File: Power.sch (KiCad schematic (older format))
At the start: 53 parts, among them J1 Conn_01x02, J2 Conn_01x02, U2 A4403, U3 TPS54531, U4 AP7361C-33E-13

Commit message: added resistor numbers
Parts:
- gave numbers to parts that had none: 34

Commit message: small revisions
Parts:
- removed D6: D_Schottky, symbol Device:D_Schottky
- added JP?: Jumper_3_Open, symbol Jumper:Jumper_3_Open
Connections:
- net labels added: 5V_INT
- wire segments 203 -> 204
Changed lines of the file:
@@
 	0    1    1    0
 $EndComp
-Wire Wire Line
-	9250 3900 9400 3900
 Connection ~ 9250 3900
-$Comp
-L power:+5V #PWR038
-U 1 1 5FBBF8B1
-P 10100 3850
-F 0 "#PWR038" H 10100 3700 50  0001 C CNN
-F 1 "+5V" H 10115 4023 50  0000 C CNN
-F 2 "" H 10100 3850 50  0001 C CNN
-F 3 "" H 10100 3850 50  0001 C CNN
-	1    10100 3850
-	1    0    0    -1
-$EndComp
-Wire Wire Line
-	10100 3850 10100 3900
 Wire Wire Line
 	10100 3900 9850 3900
-$Comp
-L Device:D_Schottky D6
-U 1 1 5FBC1E83
-P 9050 3650
-F 0 "D6" H 9050 3433 50  0000 C CNN
-F 1 "D_Schottky" H 9050 3524 50  0000 C CNN
-F 2 "" H 9050 3650 50  0001 C CNN
-F 3 "~" H 9050 3650 50  0001 C CNN
-	1    9050 3650
-	-1   0    0    1
-$EndComp
-Wire Wire Line
-	9200 3650 9400 3650
-Wire Wire Line
-	9400 3650 9400 3900
-Connection ~ 9400 3900
-Wire Wire Line
-	9400 3900 9550 3900
-Text GLabel 8700 3650 0    50   Input ~ 0
-5V_USB
-Wire Wire Line
-	8700 3650 8900 3650
 $Comp
 L power:+5V #PWR032
@@
 	9750 1100 9750 1000
 Connection ~ 9450 1100
+Text GLabel 10100 3900 2    50   Input ~ 0
+5V_INT
+$Comp
+L power:+5V #PWR?
+U 1 1 5FA47275
+P 10350 2950
+F 0 "#PWR?" H 10350 2800 50  0001 C CNN
+F 1 "+5V" H 10365 3123 50  0000 C CNN
+F 2 "" H 10350 2950 50  0001 C CNN
+F 3 "" H 10350 2950 50  0001 C CNN
+	1    10350 2950
+	1    0    0    -1
+$EndComp
+$Comp
+L Jumper:Jumper_3_Open JP?
+U 1 1 5FA47DE8
+P 9950 3050
+F 0 "JP?" V 9996 3137 50  0000 L CNN
+F 1 "Jumper_3_Open" V 9905 3137 50  0000 L CNN
+F 2 "" H 9950 3050 50  0001 C CNN
+F 3 "~" H 9950 3050 50  0001 C CNN
+	1    9950 3050
+	0    -1   -1   0
+$EndComp
+Text GLabel 9850 3450 0    50   Input ~ 0
+5V_USB
+Text GLabel 9850 2700 0    50   Input ~ 0
+5V_INT
+Wire Wire Line
+	9850 3450 9950 3450
+Wire Wire Line
+	9950 3450 9950 3300
+Wire Wire Line
+	9950 2800 9950 2700
+Wire Wire Line
+	9950 2700 9850 2700
+Wire Wire Line
+	10100 3050 10350 3050
+Wire Wire Line
+	10350 3050 10350 2950
+Wire Wire Line
+	9250 3900 9550 3900
 $EndSCHEMATC

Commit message: Completed Labelling of Schematic - All nets attached
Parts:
- added D? (x3): LED, symbol Device:LED
- added R? (x3): 2.2k, symbol Device:R_US
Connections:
- wire segments 204 -> 216
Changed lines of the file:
@@
 Wire Wire Line
 	9250 3900 9550 3900
+$Comp
+L Device:LED D?
+U 1 1 604875E7
+P 1700 5650
+F 0 "D?" V 1739 5532 50  0000 R CNN
+F 1 "LED" V 1648 5532 50  0000 R CNN
+F 2 "" H 1700 5650 50  0001 C CNN
+F 3 "~" H 1700 5650 50  0001 C CNN
+	1    1700 5650
+	0    -1   -1   0
+$EndComp
+$Comp
+L Device:R_US R?
+U 1 1 604887E0
+P 1700 5250
+F 0 "R?" H 1768 5296 50  0000 L CNN
+F 1 "2.2k" H 1768 5205 50  0000 L CNN
+F 2 "" V 1740 5240 50  0001 C CNN
+F 3 "~" H 1700 5250 50  0001 C CNN
+	1    1700 5250
+	1    0    0    -1
+$EndComp
+$Comp
+L power:GND #PWR?
+U 1 1 60488EDC
+P 1700 5950
+F 0 "#PWR?" H 1700 5700 50  0001 C CNN
+F 1 "GND" H 1705 5777 50  0000 C CNN
+F 2 "" H 1700 5950 50  0001 C CNN
+F 3 "" H 1700 5950 50  0001 C CNN
+	1    1700 5950
+	1    0    0    -1
+$EndComp
+Wire Wire Line
+	1700 5950 1700 5800
+Wire Wire Line
+	1700 5500 1700 5400
+$Comp
+L Device:LED D?
+U 1 1 604A7613
+P 2150 5650
+F 0 "D?" V 2189 5532 50  0000 R CNN
+F 1 "LED" V 2098 5532 50  0000 R CNN
+F 2 "" H 2150 5650 50  0001 C CNN
+F 3 "~" H 2150 5650 50  0001 C CNN
+	1    2150 5650
+	0    -1   -1   0
+$EndComp
+$Comp
+L Device:R_US R?
+U 1 1 604A7619
+P 2150 5250
+F 0 "R?" H 2218 5296 50  0000 L CNN
+F 1 "2.2k" H 2218 5205 50  0000 L CNN
+F 2 "" V 2190 5240 50  0001 C CNN
+F 3 "~" H 2150 5250 50  0001 C CNN
+	1    2150 5250
+	1    0    0    -1
+$EndComp
+$Comp
+L power:GND #PWR?
+U 1 1 604A761F
+P 2150 5950
+F 0 "#PWR?" H 2150 5700 50  0001 C CNN
+F 1 "GND" H 2155 5777 50  0000 C CNN
+F 2 "" H 2150 5950 50  0001 C CNN
+F 3 "" H 2150 5950 50  0001 C CNN
+	1    2150 5950
+	1    0    0    -1
+$EndComp
+Wire Wire Line
+	2150 5950 2150 5800
+Wire Wire Line
+	2150 5500 2150 5400
+$Comp
+L Device:LED D?
+U 1 1 604B1E4C
+P 2550 5650
+F 0 "D?" V 2589 5532 50  0000 R CNN
+F 1 "LED" V 2498 5532 50  0000 R CNN
+F 2 "" H 2550 5650 50  0001 C CNN
+F 3 "~" H 2550 5650 50  0001 C CNN
+	1    2550 5650
+	0    -1   -1   0
+$EndComp
+$Comp
+L Device:R_US R?
+U 1 1 604B1E52
+P 2550 5250
+F 0 "R?" H 2618 5296 50  0000 L CNN
+F 1 "2.2k" H 2618 5205 50  0000 L CNN
+F 2 "" V 2590 5240 50  0001 C CNN
+F 3 "~" H 2550 5250 50  0001 C CNN
+	1    2550 5250
+	1    0    0    -1
+$EndComp
+$Comp
+L power:GND #PWR?
+U 1 1 604B1E58
+P 2550 5950
+F 0 "#PWR?" H 2550 5700 50  0001 C CNN
+F 1 "GND" H 2555 5777 50  0000 C CNN
+F 2 "" H 2550 5950 50  0001 C CNN
+F 3 "" H 2550 5950 50  0001 C CNN
+	1    2550 5950
+	1    0    0    -1
+$EndComp
+Wire Wire Line
+	2550 5950 2550 5800
+Wire Wire Line
+	2550 5500 2550 5400
+Text GLabel 1650 4850 0    50   Input ~ 0
+VIN
+Wire Wire Line
+	1650 4850 1700 4850
+Wire Wire Line
+	1700 4850 1700 5100
+Text GLabel 2050 4700 0    50   Input ~ 0
+VIN_BED
+Wire Wire Line
+	2050 4700 2150 4700
+Wire Wire Line
+	2150 4700 2150 5100
+Text GLabel 2450 4600 0    50   Input ~ 0
+5V_USB
+Wire Wire Line
+	2450 4600 2550 4600
+Wire Wire Line
+	2550 4600 2550 5100
 $EndSCHEMATC

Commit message: added raspberry pi header
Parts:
- gave numbers to parts that had none: 7
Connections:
- no-connect marks 0 -> 1
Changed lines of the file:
@@
 5V_INT
 $Comp
-L power:+5V #PWR?
+L power:+5V #PWR0157
 U 1 1 5FA47275
 P 10350 2950
-F 0 "#PWR?" H 10350 2800 50  0001 C CNN
+F 0 "#PWR0157" H 10350 2800 50  0001 C CNN
 F 1 "+5V" H 10365 3123 50  0000 C CNN
 F 2 "" H 10350 2950 50  0001 C CNN
@@
 $EndComp
 $Comp
-L Jumper:Jumper_3_Open JP?
+L Jumper:Jumper_3_Open JP22
 U 1 1 5FA47DE8
 P 9950 3050
-F 0 "JP?" V 9996 3137 50  0000 L CNN
+F 0 "JP22" V 9996 3137 50  0000 L CNN
 F 1 "Jumper_3_Open" V 9905 3137 50  0000 L CNN
 F 2 "" H 9950 3050 50  0001 C CNN
@@
 	9250 3900 9550 3900
 $Comp
-L Device:LED D?
+L Device:LED D6
 U 1 1 604875E7
 P 1700 5650
-F 0 "D?" V 1739 5532 50  0000 R CNN
+F 0 "D6" V 1739 5532 50  0000 R CNN
 F 1 "LED" V 1648 5532 50  0000 R CNN
 F 2 "" H 1700 5650 50  0001 C CNN
@@
 $EndComp
 $Comp
-L Device:R_US R?
+L Device:R_US R66
 U 1 1 604887E0
 P 1700 5250
-F 0 "R?" H 1768 5296 50  0000 L CNN
+F 0 "R66" H 1768 5296 50  0000 L CNN
 F 1 "2.2k" H 1768 5205 50  0000 L CNN
 F 2 "" V 1740 5240 50  0001 C CNN
@@
 $EndComp
 $Comp
-L power:GND #PWR?
+L power:GND #PWR038
 U 1 1 60488EDC
 P 1700 5950
-F 0 "#PWR?" H 1700 5700 50  0001 C CNN
+F 0 "#PWR038" H 1700 5700 50  0001 C CNN
 F 1 "GND" H 1705 5777 50  0000 C CNN
 F 2 "" H 1700 5950 50  0001 C CNN
@@
 	1700 5500 1700 5400
 $Comp
-L Device:LED D?
+L Device:LED D7
 U 1 1 604A7613
 P 2150 5650
-F 0 "D?" V 2189 5532 50  0000 R CNN
+F 0 "D7" V 2189 5532 50  0000 R CNN
 F 1 "LED" V 2098 5532 50  0000 R CNN
 F 2 "" H 2150 5650 50  0001 C CNN
@@
 $EndComp
 $Comp
-L Device:R_US R?
+L Device:R_US R67
 U 1 1 604A7619
 P 2150 5250
-F 0 "R?" H 2218 5296 50  0000 L CNN
+F 0 "R67" H 2218 5296 50  0000 L CNN
 F 1 "2.2k" H 2218 5205 50  0000 L CNN
 F 2 "" V 2190 5240 50  0001 C CNN
@@
 $EndComp
 $Comp
-L power:GND #PWR?
+L power:GND #PWR0155
 U 1 1 604A761F
 P 2150 5950
-F 0 "#PWR?" H 2150 5700 50  0001 C CNN
+F 0 "#PWR0155" H 2150 5700 50  0001 C CNN
 F 1 "GND" H 2155 5777 50  0000 C CNN
 F 2 "" H 2150 5950 50  0001 C CNN
@@
 	2150 5500 2150 5400
 $Comp
-L Device:LED D?
+L Device:LED D8
 U 1 1 604B1E4C
 P 2550 5650
-F 0 "D?" V 2589 5532 50  0000 R CNN
+F 0 "D8" V 2589 5532 50  0000 R CNN
 F 1 "LED" V 2498 5532 50  0000 R CNN
 F 2 "" H 2550 5650 50  0001 C CNN
@@
 $EndComp
 $Comp
-L Device:R_US R?
+L Device:R_US R68
 U 1 1 604B1E52
 P 2550 5250
-F 0 "R?" H 2618 5296 50  0000 L CNN
+F 0 "R68" H 2618 5296 50  0000 L CNN
 F 1 "2.2k" H 2618 5205 50  0000 L CNN
 F 2 "" V 2590 5240 50  0001 C CNN
@@
 $EndComp
 $Comp
-L power:GND #PWR?
+L power:GND #PWR0156
 U 1 1 604B1E58
 P 2550 5950
-F 0 "#PWR?" H 2550 5700 50  0001 C CNN
+F 0 "#PWR0156" H 2550 5700 50  0001 C CNN
 F 1 "GND" H 2555 5777 50  0000 C CNN
 F 2 "" H 2550 5950 50  0001 C CNN
@@
 Wire Wire Line
 	2550 4600 2550 5100
+NoConn ~ 6400 4050
 $EndSCHEMATC

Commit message: assigned some footprints
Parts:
- C24, C25, C26, C27, C28, C29, C32, C38, C41, C53: footprint (none) -> Capacitor_SMD:C_0603_1608Metric_Pad1.05x0.95mm_HandSolder
- C36: footprint (none) -> Capacitor_SMD:CP_Elec_6.3x7.7
- C37, C42, C46, C50, C52: footprint (none) -> Capacitor_SMD:C_0805_2012Metric_Pad1.15x1.40mm_HandSolder
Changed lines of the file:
@@
 F 0 "C24" H 1892 2496 50  0000 L CNN
 F 1 "100nF" H 1892 2405 50  0000 L CNN
-F 2 "" H 1800 2450 50  0001 C CNN
+F 2 "Capacitor_SMD:C_0603_1608Metric_Pad1.05x0.95mm_HandSolder" H 1800 2450 50  0001 C CNN
 F 3 "~" H 1800 2450 50  0001 C CNN
 	1    1800 2450
@@
 F 0 "C27" H 2492 2496 50  0000 L CNN
 F 1 "100nF" H 2492 2405 50  0000 L CNN
-F 2 "" H 2400 2450 50  0001 C CNN
+F 2 "Capacitor_SMD:C_0603_1608Metric_Pad1.05x0.95mm_HandSolder" H 2400 2450 50  0001 C CNN
 F 3 "~" H 2400 2450 50  0001 C CNN
 	1    2400 2450
@@
 F 0 "C26" H 1892 4046 50  0000 L CNN
 F 1 "100nF" H 1892 3955 50  0000 L CNN
-F 2 "" H 1800 4000 50  0001 C CNN
+F 2 "Capacitor_SMD:C_0603_1608Metric_Pad1.05x0.95mm_HandSolder" H 1800 4000 50  0001 C CNN
 F 3 "~" H 1800 4000 50  0001 C CNN
 	1    1800 4000
@@
 F 0 "C29" H 2492 4046 50  0000 L CNN
 F 1 "100nF" H 2492 3955 50  0000 L CNN
-F 2 "" H 2400 4000 50  0001 C CNN
+F 2 "Capacitor_SMD:C_0603_1608Metric_Pad1.05x0.95mm_HandSolder" H 2400 4000 50  0001 C CNN
 F 3 "~" H 2400 4000 50  0001 C CNN
 	1    2400 4000
@@
 F 0 "C25" H 1892 3246 50  0000 L CNN
 F 1 "100nF" H 1892 3155 50  0000 L CNN
-F 2 "" H 1800 3200 50  0001 C CNN
+F 2 "Capacitor_SMD:C_0603_1608Metric_Pad1.05x0.95mm_HandSolder" H 1800 3200 50  0001 C CNN
 F 3 "~" H 1800 3200 50  0001 C CNN
 	1    1800 3200
@@
 F 0 "C28" H 2492 3246 50  0000 L CNN
 F 1 "100nF" H 2492 3155 50  0000 L CNN
-F 2 "" H 2400 3200 50  0001 C CNN
+F 2 "Capacitor_SMD:C_0603_1608Metric_Pad1.05x0.95mm_HandSolder" H 2400 3200 50  0001 C CNN
 F 3 "~" H 2400 3200 50  0001 C CNN
 	1    2400 3200
@@
 F 0 "C32" V 5592 4146 50  0000 L BNN
 F 1 "100nF" V 5592 4055 50  0000 R BNN
-F 2 "" H 5500 4100 50  0001 C CNN
+F 2 "Capacitor_SMD:C_0603_1608Metric_Pad1.05x0.95mm_HandSolder" H 5500 4100 50  0001 C CNN
 F 3 "~" H 5500 4100 50  0001 C CNN
 	1    5500 4100
@@
 F 0 "C42" V 6192 5996 50  0000 L BNN
 F 1 "10uF" V 6192 5905 50  0000 R BNN
-F 2 "" H 6100 5950 50  0001 C CNN
+F 2 "Capacitor_SMD:C_0805_2012Metric_Pad1.15x1.40mm_HandSolder" H 6100 5950 50  0001 C CNN
 F 3 "~" H 6100 5950 50  0001 C CNN
 	1    6100 5950
@@
 F 0 "C46" V 7692 5996 50  0000 L BNN
 F 1 "10uF" V 7692 5905 50  0000 R BNN
-F 2 "" H 7600 5950 50  0001 C CNN
+F 2 "Capacitor_SMD:C_0805_2012Metric_Pad1.15x1.40mm_HandSolder" H 7600 5950 50  0001 C CNN
 F 3 "~" H 7600 5950 50  0001 C CNN
 	1    7600 5950
@@
 F 0 "C37" V 5492 1346 50  0000 L BNN
 F 1 "10uF" V 5492 1255 50  0000 R BNN
-F 2 "" H 5400 1300 50  0001 C CNN
+F 2 "Capacitor_SMD:C_0805_2012Metric_Pad1.15x1.40mm_HandSolder" H 5400 1300 50  0001 C CNN
 F 3 "~" H 5400 1300 50  0001 C CNN
 	1    5400 1300
@@
 F 0 "C38" V 5642 1346 50  0000 L BNN
 F 1 "100nF" V 5642 1255 50  0000 R BNN
-F 2 "" H 5550 1300 50  0001 C CNN
+F 2 "Capacitor_SMD:C_0603_1608Metric_Pad1.05x0.95mm_HandSolder" H 5550 1300 50  0001 C CNN
 F 3 "~" H 5550 1300 50  0001 C CNN
 	1    5550 1300
@@
 F 0 "C36" V 5341 1346 50  0000 L BNN
 F 1 "100uF" V 5341 1255 50  0000 R BNN
-F 2 "" H 5250 1300 50  0001 C CNN
+F 2 "Capacitor_SMD:CP_Elec_6.3x7.7" H 5250 1300 50  0001 C CNN
 F 3 "~" H 5250 1300 50  0001 C CNN
 	1    5250 1300
@@
 F 0 "C41" V 6192 1896 50  0000 L BNN
 F 1 "100nF" V 6192 1805 50  0000 R BNN
-F 2 "" H 6100 1850 50  0001 C CNN
+F 2 "Capacitor_SMD:C_0603_1608Metric_Pad1.05x0.95mm_HandSolder" H 6100 1850 50  0001 C CNN
 F 3 "~" H 6100 1850 50  0001 C CNN
 	1    6100 1850
@@
 F 0 "C50" V 9242 1346 50  0000 L BNN
 F 1 "10uF" V 9242 1255 50  0000 R BNN
-F 2 "" H 9150 1300 50  0001 C CNN
+F 2 "Capacitor_SMD:C_0805_2012Metric_Pad1.15x1.40mm_HandSolder" H 9150 1300 50  0001 C CNN
 F 3 "~" H 9150 1300 50  0001 C CNN
 	1    9150 1300
@@
 F 0 "C52" V 9392 1346 50  0000 L BNN
 F 1 "10uF" V 9392 1255 50  0000 R BNN
-F 2 "" H 9300 1300 50  0001 C CNN
+F 2 "Capacitor_SMD:C_0805_2012Metric_Pad1.15x1.40mm_HandSolder" H 9300 1300 50  0001 C CNN
 F 3 "~" H 9300 1300 50  0001 C CNN
 	1    9300 1300
@@
 F 0 "C53" V 9542 1346 50  0000 L BNN
 F 1 "100nF" V 9542 1255 50  0000 R BNN
-F 2 "" H 9450 1300 50  0001 C CNN
+F 2 "Capacitor_SMD:C_0603_1608Metric_Pad1.05x0.95mm_HandSolder" H 9450 1300 50  0001 C CNN
 F 3 "~" H 9450 1300 50  0001 C CNN
 	1    9450 1300

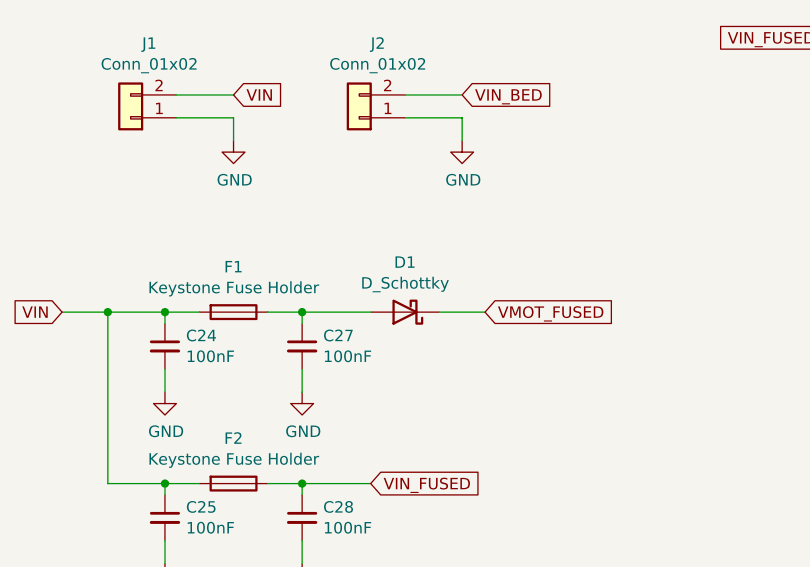
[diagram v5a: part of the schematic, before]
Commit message: associated more footprints
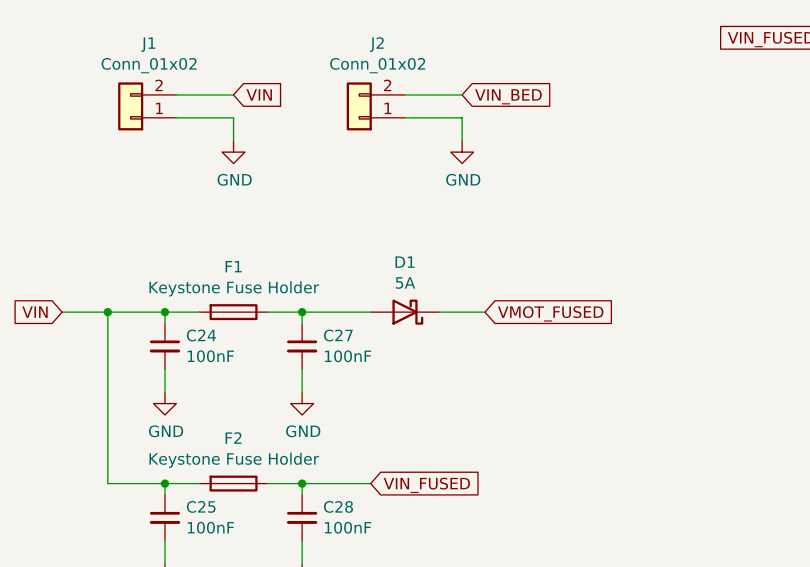
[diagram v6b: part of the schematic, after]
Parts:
- C30, C31: footprint (none) -> Capacitor_SMD:C_0805_2012Metric_Pad1.15x1.40mm_HandSolder
- C39, C40, C43, C44, C45, C47, C48, C49, C51: footprint (none) -> Capacitor_SMD:C_0603_1608Metric_Pad1.05x0.95mm_HandSolder
- D1: value D_Schottky -> 5A; footprint (none) -> Diode_SMD:D_SMA_Handsoldering
- D2, D3, D4: footprint (none) -> Diode_SMD:D_SOD-123F
- D5: footprint (none) -> Diode_SMD:D_SMC_Handsoldering
- D6, D7, D8: footprint (none) -> LED_SMD:LED_0603_1608Metric_Pad1.05x0.95mm_HandSolder
- F1, F2, F3, F4: footprint (none) -> Fuse:Fuseholder_Blade_Mini_Keystone_3568
- JP22: footprint (none) -> Connector_PinHeader_2.54mm:PinHeader_1x03_P2.54mm_Vertical
- JP3: footprint (none) -> Connector_PinHeader_2.54mm:PinHeader_1x02_P2.54mm_Vertical

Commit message: Added more footprints
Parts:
- L2, L3: footprint (none) -> Inductor_SMD:L_Vishay_IHLP-2525
- R10, R11, R12, R13, R6, R66, R67, R68, R7: footprint (none) -> Resistor_SMD:R_0603_1608Metric_Pad1.05x0.95mm_HandSolder
- R8, R9: footprint (none) -> Resistor_SMD:R_1206_3216Metric_Pad1.42x1.75mm_HandSolder
- U2: footprint (none) -> Package_DFN_QFN:QFN-16-1EP_4x4mm_P0.65mm_EP2.7x2.7mm_ThermalVias
- U3: footprint (none) -> Package_SO:TI_SO-PowerPAD-8_ThermalVias
- U4: footprint (none) -> Package_TO_SOT_SMD:SOT-223
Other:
- note added: "IHLP2525CZER100M11"
- note added: "IHLP2525EZER4R7M01"
- note added: "SOT-223\n"
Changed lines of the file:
@@
 F 0 "U2" H 6750 1665 50  0000 C CNN
 F 1 "A4403" H 6750 1574 50  0000 C CNN
-F 2 "" H 7200 450 50  0001 C CNN
+F 2 "Package_DFN_QFN:QFN-16-1EP_4x4mm_P0.65mm_EP2.7x2.7mm_ThermalVias" H 7200 450 50  0001 C CNN
 F 3 "" H 7200 450 50  0001 C CNN
 	1    6750 1250
@@
 F 0 "U4" H 6900 6415 50  0000 C CNN
 F 1 "AP7361C-33E-13" H 6900 6324 50  0000 C CNN
-F 2 "" H 7150 5850 50  0001 C CNN
+F 2 "Package_TO_SOT_SMD:SOT-223" H 7150 5850 50  0001 C CNN
 F 3 "" H 7150 5850 50  0001 C CNN
 	1    6900 5950
@@
 F 0 "U3" H 6850 4365 50  0000 C CNN
 F 1 "TPS54531" H 6850 4274 50  0000 C CNN
-F 2 "" H 7200 3450 50  0001 C CNN
+F 2 "Package_SO:TI_SO-PowerPAD-8_ThermalVias" H 7200 3450 50  0001 C CNN
 F 3 "" H 7200 3450 50  0001 C CNN
 	1    6850 4000
@@
 F 0 "L2" V 8540 3900 50  0000 C CNN
 F 1 "4.7uH" V 8449 3900 50  0000 C CNN
-F 2 "" H 8350 3900 50  0001 C CNN
+F 2 "Inductor_SMD:L_Vishay_IHLP-2525" H 8350 3900 50  0001 C CNN
 F 3 "~" H 8350 3900 50  0001 C CNN
 	1    8350 3900
@@
 F 0 "R10" V 8618 4096 50  0000 L BNN
 F 1 "10.2k" V 8618 4005 50  0000 R BNN
-F 2 "" H 8550 4050 50  0001 C CNN
+F 2 "Resistor_SMD:R_0603_1608Metric_Pad1.05x0.95mm_HandSolder" H 8550 4050 50  0001 C CNN
 F 3 "~" H 8550 4050 50  0001 C CNN
 	1    8550 4050
@@
 F 0 "R11" V 8618 4546 50  0000 L BNN
 F 1 "1.96k" V 8618 4455 50  0000 R BNN
-F 2 "" H 8550 4500 50  0001 C CNN
+F 2 "Resistor_SMD:R_0603_1608Metric_Pad1.05x0.95mm_HandSolder" H 8550 4500 50  0001 C CNN
 F 3 "~" H 8550 4500 50  0001 C CNN
 	1    8550 4500
@@
 F 0 "R6" V 5818 4796 50  0000 L BNN
 F 1 "37.4k" V 5818 4705 50  0000 R BNN
-F 2 "" H 5750 4750 50  0001 C CNN
+F 2 "Resistor_SMD:R_0603_1608Metric_Pad1.05x0.95mm_HandSolder" H 5750 4750 50  0001 C CNN
 F 3 "~" H 5750 4750 50  0001 C CNN
 	1    5750 4750
@@
 F 0 "R7" V 6068 1346 50  0000 L BNN
 F 1 "200k" V 6068 1255 50  0000 R BNN
-F 2 "" H 6000 1300 50  0001 C CNN
+F 2 "Resistor_SMD:R_0603_1608Metric_Pad1.05x0.95mm_HandSolder" H 6000 1300 50  0001 C CNN
 F 3 "~" H 6000 1300 50  0001 C CNN
 	1    6000 1300
@@
 F 0 "L3" V 8640 1100 50  0000 C CNN
 F 1 "10uH" V 8549 1100 50  0000 C CNN
-F 2 "" H 8450 1100 50  0001 C CNN
+F 2 "Inductor_SMD:L_Vishay_IHLP-2525" H 8450 1100 50  0001 C CNN
 F 3 "~" H 8450 1100 50  0001 C CNN
 	1    8450 1100
@@
 F 0 "R8" V 7918 1596 50  0000 L BNN
 F 1 "0.1" V 7918 1505 50  0000 R BNN
-F 2 "" H 7850 1550 50  0001 C CNN
+F 2 "Resistor_SMD:R_1206_3216Metric_Pad1.42x1.75mm_HandSolder" H 7850 1550 50  0001 C CNN
 F 3 "~" H 7850 1550 50  0001 C CNN
 	1    7850 1550
@@
 F 0 "R9" V 7918 1696 50  0000 L BNN
 F 1 "0.1" V 7918 1605 50  0000 R BNN
-F 2 "" H 7850 1650 50  0001 C CNN
+F 2 "Resistor_SMD:R_1206_3216Metric_Pad1.42x1.75mm_HandSolder" H 7850 1650 50  0001 C CNN
 F 3 "~" H 7850 1650 50  0001 C CNN
 	1    7850 1650
@@
 F 0 "R12" V 8818 1346 50  0000 L BNN
 F 1 "10.5k" V 8818 1255 50  0000 R BNN
-F 2 "" H 8750 1300 50  0001 C CNN
+F 2 "Resistor_SMD:R_0603_1608Metric_Pad1.05x0.95mm_HandSolder" H 8750 1300 50  0001 C CNN
 F 3 "~" H 8750 1300 50  0001 C CNN
 	1    8750 1300
@@
 F 0 "R13" V 8818 1946 50  0000 L BNN
 F 1 "750" V 8818 1855 50  0000 R BNN
-F 2 "" H 8750 1900 50  0001 C CNN
+F 2 "Resistor_SMD:R_0603_1608Metric_Pad1.05x0.95mm_HandSolder" H 8750 1900 50  0001 C CNN
 F 3 "~" H 8750 1900 50  0001 C CNN
 	1    8750 1900
@@
 F 0 "R66" H 1768 5296 50  0000 L CNN
 F 1 "2.2k" H 1768 5205 50  0000 L CNN
-F 2 "" V 1740 5240 50  0001 C CNN
+F 2 "Resistor_SMD:R_0603_1608Metric_Pad1.05x0.95mm_HandSolder" V 1740 5240 50  0001 C CNN
 F 3 "~" H 1700 5250 50  0001 C CNN
 	1    1700 5250
@@
 F 0 "R67" H 2218 5296 50  0000 L CNN
 F 1 "2.2k" H 2218 5205 50  0000 L CNN
-F 2 "" V 2190 5240 50  0001 C CNN
+F 2 "Resistor_SMD:R_0603_1608Metric_Pad1.05x0.95mm_HandSolder" V 2190 5240 50  0001 C CNN
 F 3 "~" H 2150 5250 50  0001 C CNN
 	1    2150 5250
@@
 F 0 "R68" H 2618 5296 50  0000 L CNN
 F 1 "2.2k" H 2618 5205 50  0000 L CNN
-F 2 "" V 2590 5240 50  0001 C CNN
+F 2 "Resistor_SMD:R_0603_1608Metric_Pad1.05x0.95mm_HandSolder" V 2590 5240 50  0001 C CNN
 F 3 "~" H 2550 5250 50  0001 C CNN
 	1    2550 5250
@@
 	1    0    0    -1
 $EndComp
+Text Notes 8100 800  0    50   ~ 0
+IHLP2525CZER100M11
+Text Notes 8150 3600 0    50   ~ 0
+IHLP2525EZER4R7M01
+Text Notes 7050 5400 0    50   ~ 0
+SOT-223\n
 $EndSCHEMATC
